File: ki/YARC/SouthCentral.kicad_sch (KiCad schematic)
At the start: 9 parts, among them U104 74LS86, U83 74LS139, U84 74LS157, U85 74LS157, U86 74LS157, U87 74LS138, U88 74HC00, U89 74LS157, U90 74LS157

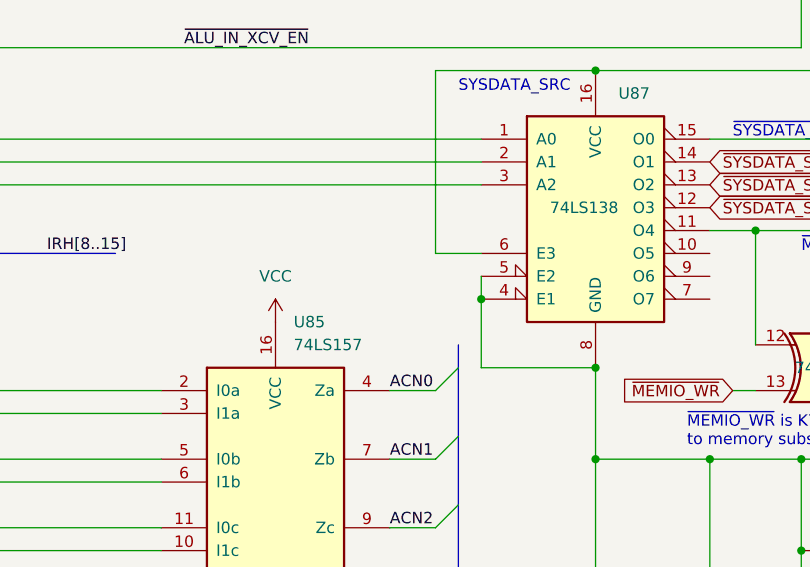
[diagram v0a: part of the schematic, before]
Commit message: Ongoing corrections. Document the Nano's sysbus enable control for the first time.
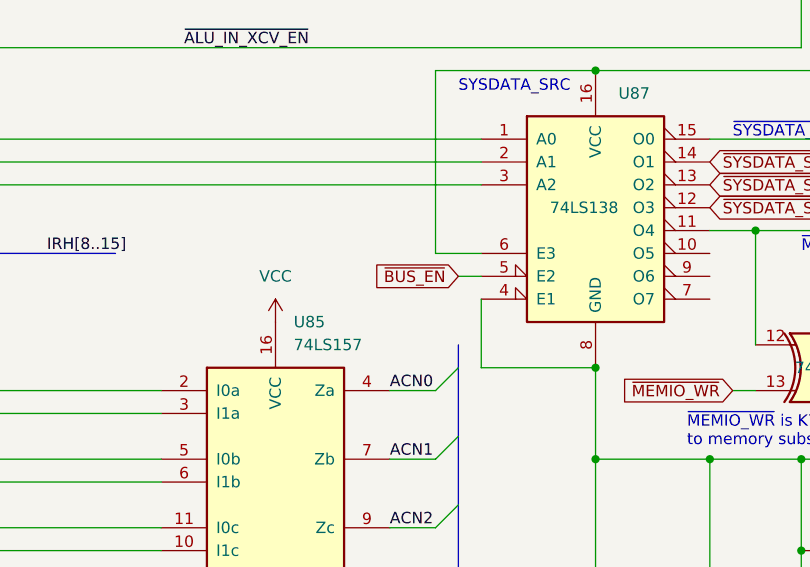
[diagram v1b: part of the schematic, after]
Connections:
- net GND: no longer U87.5 (E2)
- new net ~{BUS_EN}: U87.5 (E2)
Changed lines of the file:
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@@
   (junction (at 182.88 167.64) (diameter 0) (color 0 0 0 0)
   )
-  (junction (at 129.54 149.86) (diameter 0) (color 0 0 0 0)
-  )
   (junction (at 180.34 157.48) (diameter 0) (color 0 0 0 0)
   )
@@
     (stroke (width 0) (type default) (color 0 0 0 0))
   )
+  (wire (pts (xy 129.54 147.32) (xy 127 147.32))
+    (stroke (width 0) (type default) (color 0 0 0 0))
+  )
   (wire (pts (xy 170.18 66.04) (xy 160.02 66.04))
     (stroke (width 0) (type default) (color 0 0 0 0))
@@
   )
   (wire (pts (xy 160.02 160.02) (xy 157.48 160.02))
-    (stroke (width 0) (type default) (color 0 0 0 0))
-  )
-  (wire (pts (xy 129.54 147.32) (xy 129.54 149.86))
     (stroke (width 0) (type default) (color 0 0 0 0))
   )
@@
     )
   )
+  (global_label "~{BUS_EN}" (shape input) (at 127 147.32 180) (fields_autoplaced)
+    (effects (font (size 1.27 1.27)) (justify right))
+    (property "Intersheet References" "${INTERSHEET_REFS}" (id 0) (at 117.3298 147.2406 0)
+      (effects (font (size 1.27 1.27)) (justify right) hide)
+    )
+  )

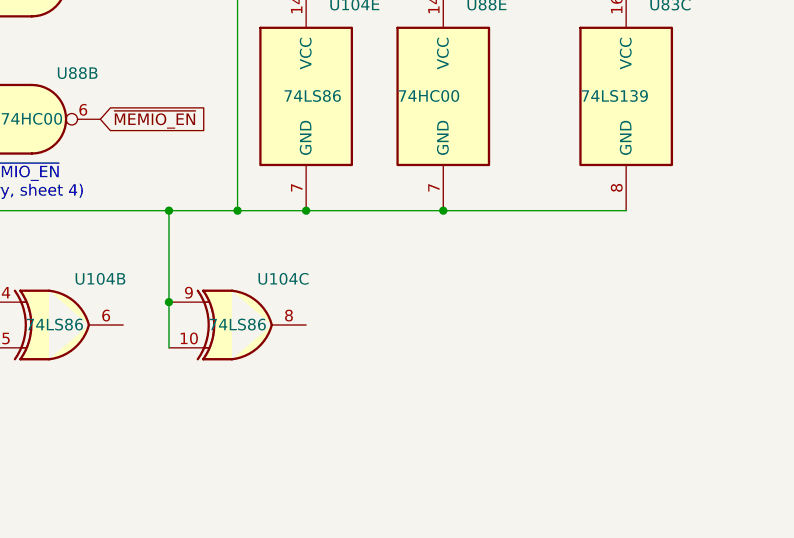
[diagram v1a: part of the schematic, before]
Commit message: Large commit. Document two hardware changes to microcode controls. Adapt Nano firmware to these changes. Significantly simplify initialization logic and make it more consistent about reset.
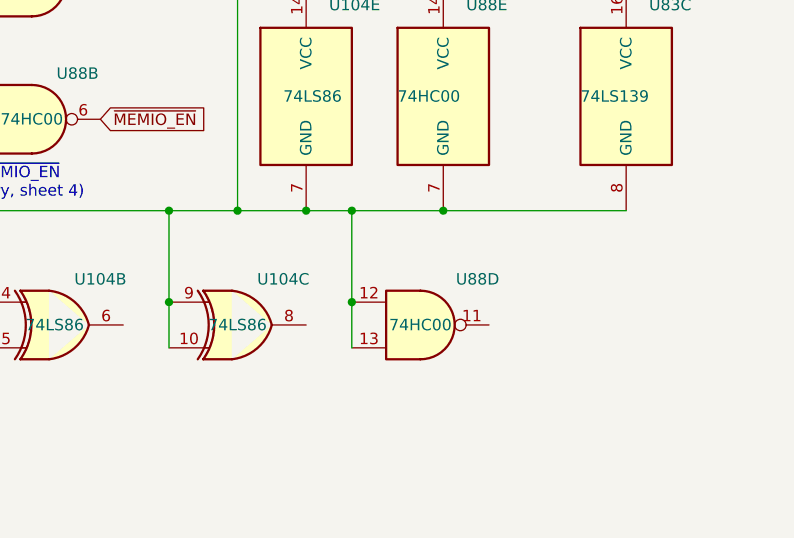
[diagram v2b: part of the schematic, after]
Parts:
- added unit 4 of U88
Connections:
- net GND: now also U88.12, U88.13
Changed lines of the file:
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@@
   (junction (at 165.1 177.8) (diameter 0) (color 0 0 0 0)
   )
+  (junction (at 223.52 167.64) (diameter 0) (color 0 0 0 0)
+  )
+  (junction (at 223.52 177.8) (diameter 0) (color 0 0 0 0)
+  )
   (junction (at 210.82 99.06) (diameter 0) (color 0 0 0 0)
   )
@@
     (stroke (width 0) (type default) (color 0 0 0 0))
   )
+  (wire (pts (xy 223.52 182.88) (xy 223.52 177.8))
+    (stroke (width 0) (type default) (color 0 0 0 0))
+  )
   (wire (pts (xy 200.66 50.8) (xy 213.36 50.8))
     (stroke (width 0) (type default) (color 0 0 0 0))
@@
     (stroke (width 0) (type default) (color 0 0 0 0))
   )
+  (wire (pts (xy 223.52 167.64) (xy 233.68 167.64))
+    (stroke (width 0) (type default) (color 0 0 0 0))
+  )
   (wire (pts (xy 129.54 149.86) (xy 129.54 157.48))
     (stroke (width 0) (type default) (color 0 0 0 0))
@@
     (stroke (width 0) (type default) (color 0 0 0 0))
   )
+  (wire (pts (xy 223.52 177.8) (xy 223.52 167.64))
+    (stroke (width 0) (type default) (color 0 0 0 0))
+  )
   (wire (pts (xy 129.54 63.5) (xy 129.54 35.56))
     (stroke (width 0) (type default) (color 0 0 0 0))
@@
     (stroke (width 0) (type default) (color 0 0 0 0))
   )
-  (wire (pts (xy 218.44 167.64) (xy 233.68 167.64))
+  (wire (pts (xy 218.44 167.64) (xy 223.52 167.64))
     (stroke (width 0) (type default) (color 0 0 0 0))
   )
@@
     (pin "7")
   )
+  (symbol (lib_id "74xx:74HC00") (at 231.14 180.34 0) (unit 4)
+    (in_bom yes) (on_board yes)
+    (property "Reference" "U88" (id 0) (at 237.49 175.26 0))
+    (property "Value" "74HC00" (id 1) (at 231.14 180.34 0))
+    (property "Footprint" "" (id 2) (at 231.14 180.34 0)
+      (effects (font (size 1.27 1.27)) hide)
+    )
+    (property "Datasheet" "http://www.ti.com/lit/gpn/sn74hc00" (id 3) (at 231.14 180.34 0)
+      (effects (font (size 1.27 1.27)) hide)
+    )
+    (pin "11")
+    (pin "12")
+    (pin "13")
+  )
   (symbol (lib_id "74xx:74LS86") (at 172.72 180.34 0) (unit 1)

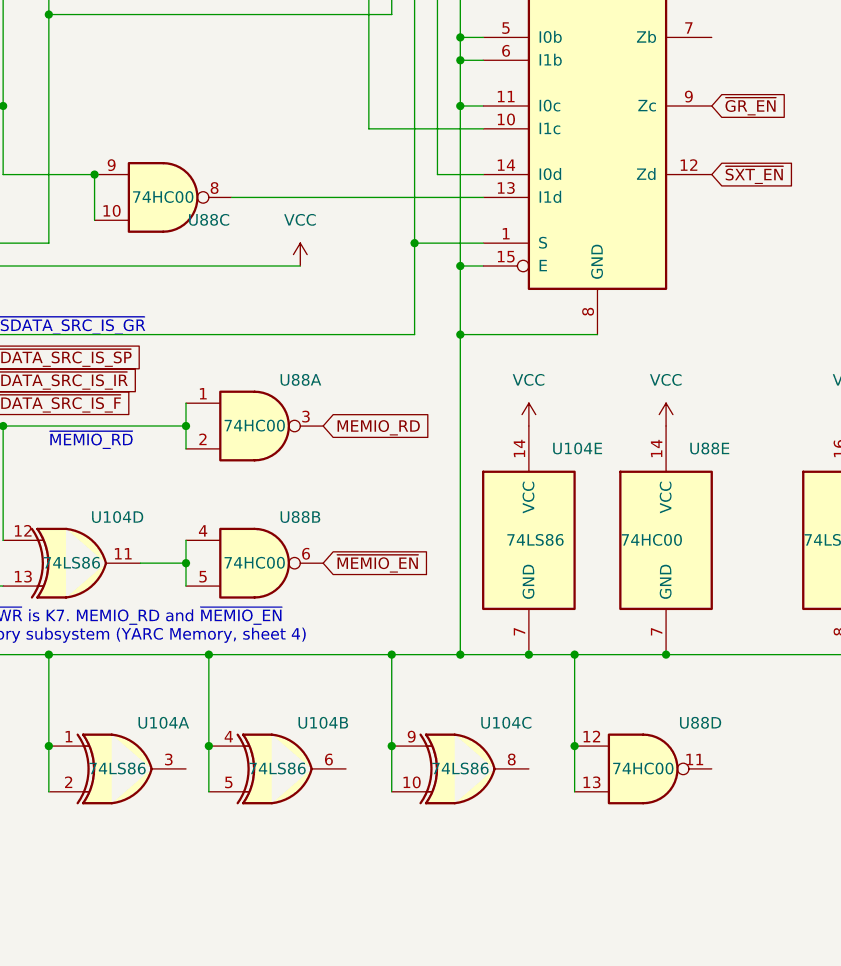
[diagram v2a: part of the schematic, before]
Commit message: Convert schematic to KiCad 7
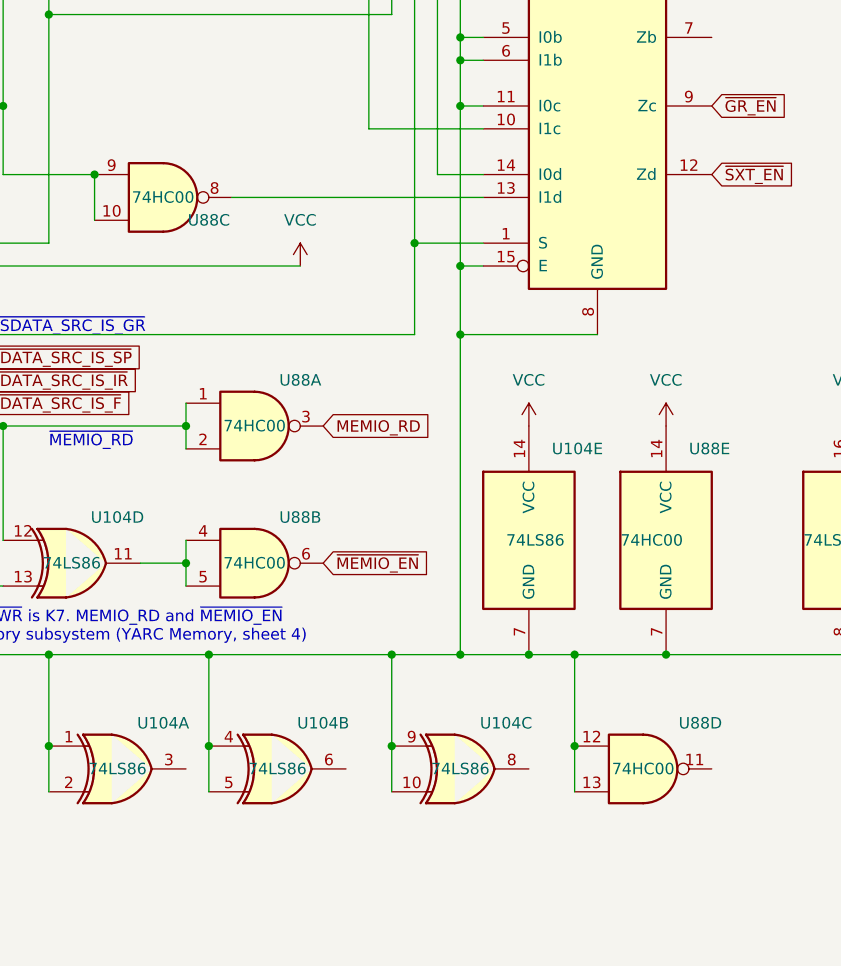
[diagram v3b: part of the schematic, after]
